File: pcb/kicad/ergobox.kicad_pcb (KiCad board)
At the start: 2 copper layers, 187.4 x 130.9 mm, 80 parts, among them SW1 SW_Push, SW10 Kailh, SW11 Kailh, SW12 Kailh, SW13 Kailh, SW14 Kailh, SW15 Kailh, SW16 Kailh, SW17 Kailh, SW18 Kailh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

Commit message: refactor: adjusts initial PCB layout to match viewlix specs
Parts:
- moved SW15 285.5 mm to (-102.5, 10.4), turned to -90 degrees
- moved C27 284.7 mm to (-111.3, 53.9), turned to -90 degrees
- moved D7 283.6 mm to (-110.1, 50.4), turned to -90 degrees
- moved R7 282.0 mm to (-109.4, 53.9), turned to -90 degrees
- moved C28 280.8 mm to (-108.8, 56.8), turned to -90 degrees
- moved U2 280.5 mm to (-107.0, 43.3), turned to -90 degrees
- moved SW20 278.4 mm to (-102.5, 28.6), turned to -90 degrees
- moved U1 278.0 mm to (-106.1, 50.5), turned to -90 degrees
- moved C4 277.8 mm to (-106.9, 59.0), turned to -90 degrees
- moved D3 276.6 mm to (-105.7, 55.6), turned to -90 degrees
- moved C2 275.9 mm to (-105.7, 61.9), turned to -90 degrees
- moved C1 275.0 mm to (-104.9, 59.0), turned to -90 degrees
- moved C18 273.1 mm to (-103.8, 61.9), turned to -90 degrees
- moved D5 269.2 mm to (-101.0, 61.8), turned to -90 degrees
- moved C26 267.9 mm to (-100.2, 65.3), turned to -90 degrees
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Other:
- board size 187.4 x 130.9 mm -> 234.6 x 145.7 mm

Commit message: feat: places kailh switches on PCB
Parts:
- moved SW20 346.7 mm to (240.6, 78.2), turned to 0 degrees
- moved SW15 308.9 mm to (204.2, 46.5), turned to 0 degrees
- moved SW16 308.4 mm to (239.5, 39.1), turned to 0 degrees
- moved SW19 280.1 mm to (205.4, 85.7), turned to 0 degrees
- moved SW14 254.8 mm to (169.0, 54.0), turned to 0 degrees
- moved SW17 248.9 mm to (140.8, 113.7), turned to 0 degrees
- moved SW9 241.8 mm to (125.5, 146.2), turned to 0 degrees
- moved SW18 227.0 mm to (170.2, 93.1), turned to 0 degrees
- moved SW13 197.1 mm to (139.7, 74.7), turned to 0 degrees
- moved C20 177.8 mm to (31.2, -39.5), turned to 0 degrees
- moved R6 173.9 mm to (28.4, -39.5), turned to 0 degrees
- moved C3 172.9 mm to (28.3, -37.5), turned to 0 degrees
- moved C8 172.0 mm to (28.3, -35.5), turned to 0 degrees
- moved C13 160.7 mm to (21.9, -29.3), turned to 0 degrees
- moved SW10 158.9 mm to (106.6, 80.0), turned to 0 degrees
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
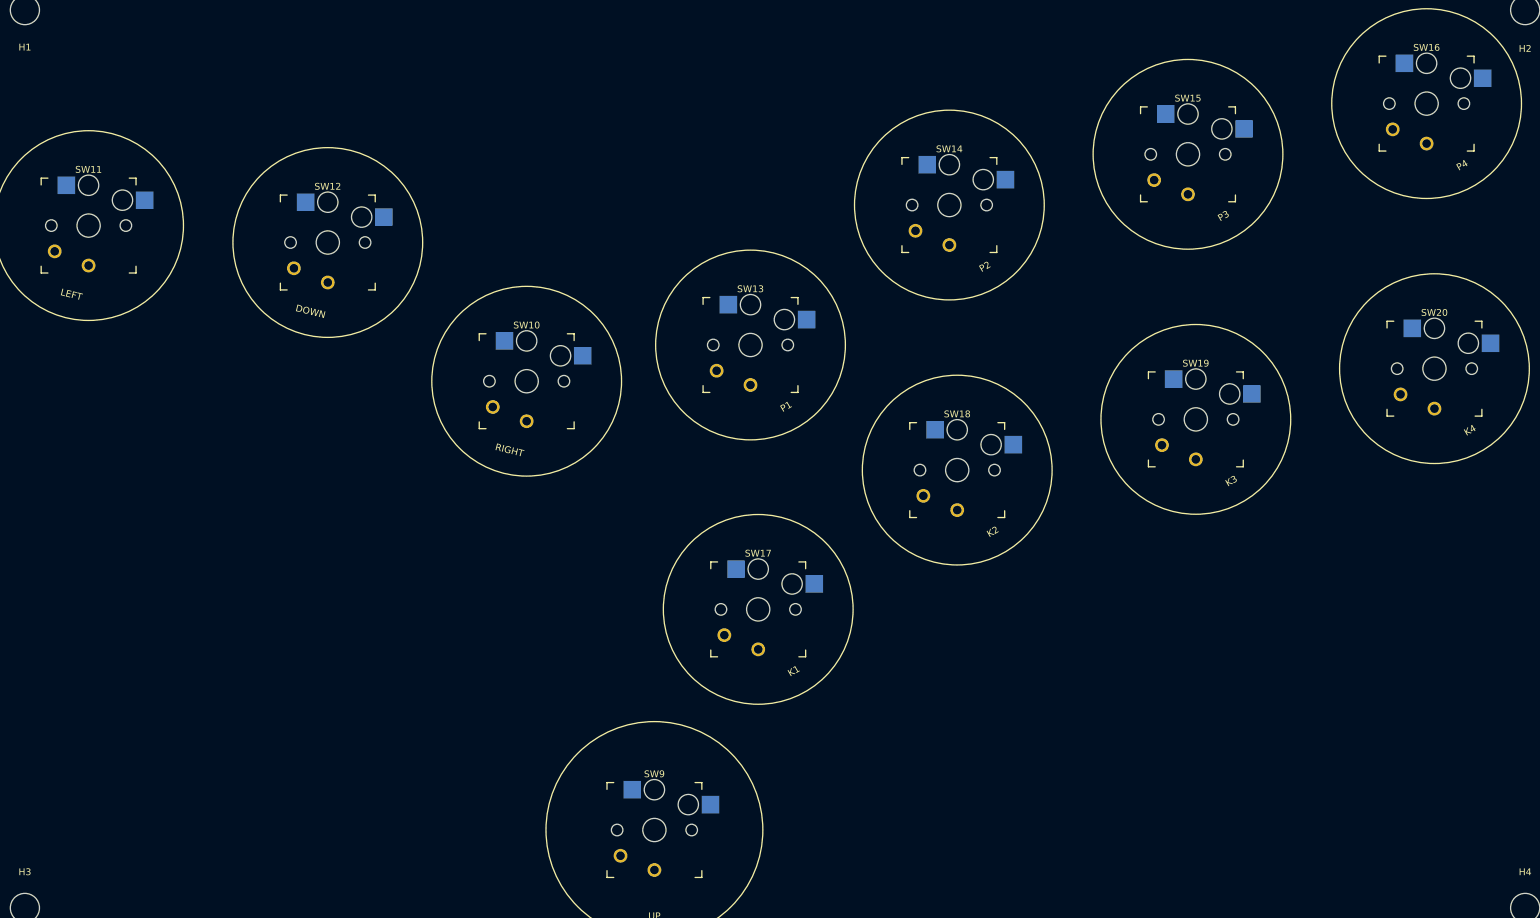
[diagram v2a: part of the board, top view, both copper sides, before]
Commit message: refactor: changes kailh footprints to hotswap non-optionals.
The kailh low footprints with optional hotswaps are not symmetric.
In the optional footprint, the hotswap switch pad goes through the RGB footpad,
so it cannot be used.
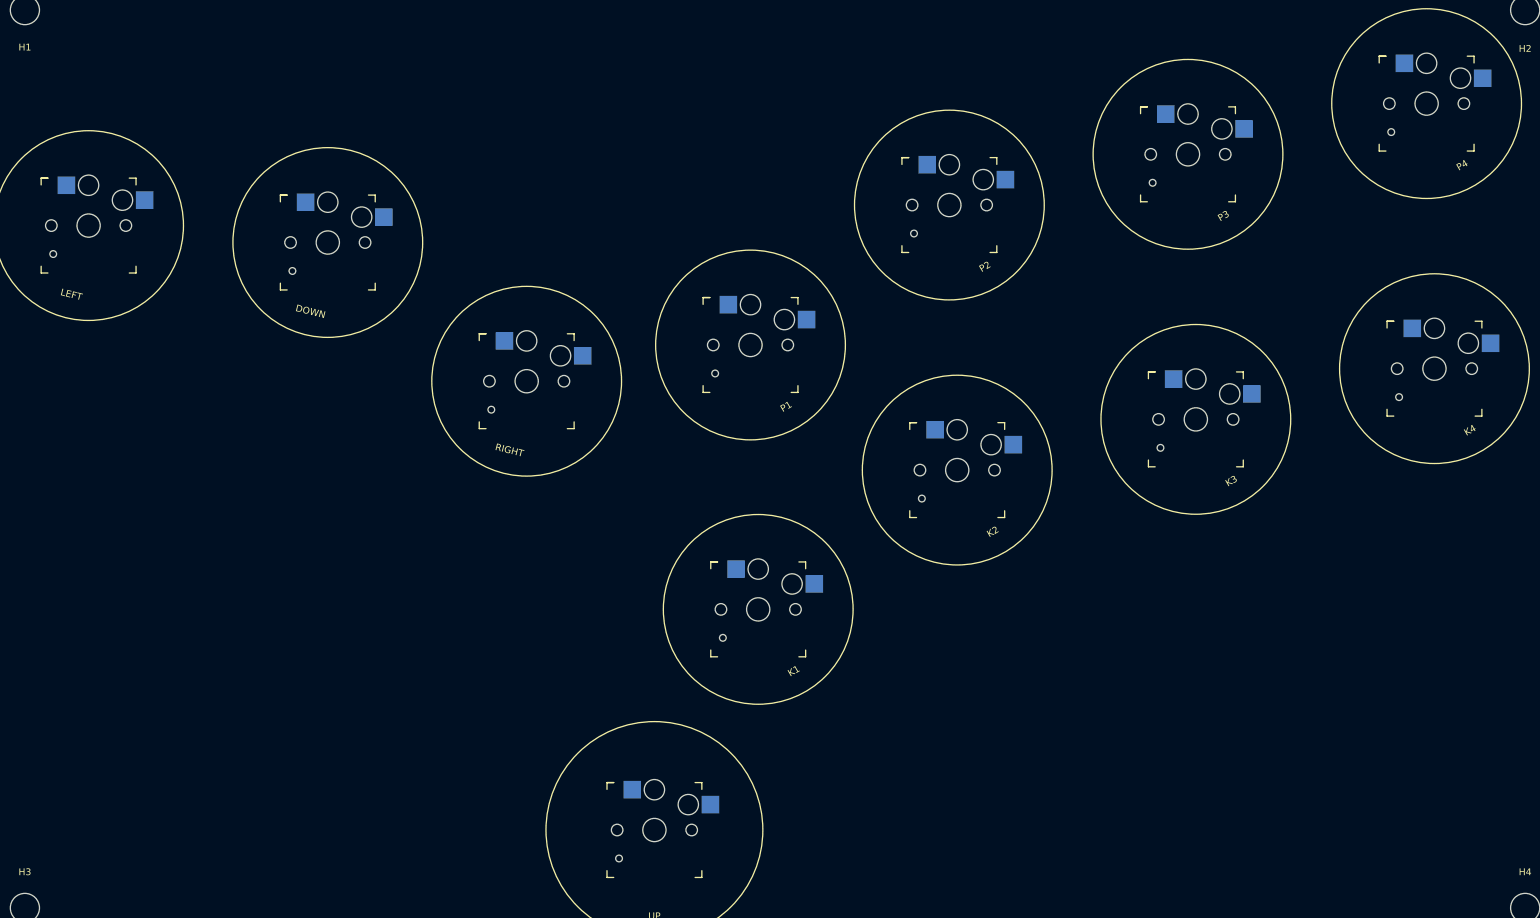
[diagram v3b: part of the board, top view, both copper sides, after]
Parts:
- SW10, SW11, SW12, SW13, SW14, SW15, SW16, SW17, SW18, SW19, SW20, SW9: footprint Keyswitches:Kailh_socket_PG1350_optional -> Keyswitches:Kailh_socket_PG1350
- turned SW10 to 180 degrees
- turned SW11 to 180 degrees
- turned SW12 to 180 degrees
- turned SW13 to 180 degrees
- turned SW14 to 180 degrees
- turned SW15 to 180 degrees
- turned SW16 to 180 degrees
- turned SW17 to 180 degrees
- turned SW18 to 180 degrees
- turned SW19 to 180 degrees
- turned SW20 to 180 degrees
- turned SW9 to 180 degrees

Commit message: feat: places per-key RGB LEDs on PCB
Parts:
- moved D7 279.8 mm to (239.5, 43.8), turned to 180 degrees
- moved D8 259.2 mm to (240.6, 82.9)
- moved D9 233.9 mm to (205.4, 90.3)
- moved D6 213.2 mm to (204.2, 51.2), turned to 180 degrees
- moved D10 209.1 mm to (170.2, 97.8)
- moved D12 206.2 mm to (125.5, 150.9)
- moved D5 201.7 mm to (169.0, 58.7), turned to 180 degrees
- moved D11 195.1 mm to (140.8, 118.4)
- moved D4 162.3 mm to (139.7, 79.4), turned to 180 degrees
- moved D3 154.6 mm to (106.6, 84.7), turned to 180 degrees
- moved D2 109.0 mm to (77.3, 64.2), turned to 180 degrees
- moved D1 83.7 mm to (42.0, 61.8), turned to 180 degrees

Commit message: feat: introduces GND plane on B.Cu
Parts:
- H5: footprint MountingHole:MountingHole_3.2mm_M3 -> MountingHole:MountingHole_4.3mm_M4
- moved H5 192.0 mm to (143.3, 25.5)
- moved H6 116.2 mm to (143.3, 157.8)
- moved USB1 75.1 mm to (61.6, 13.2), turned to 180 degrees
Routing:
- added copper zone on B.Cu, net GND
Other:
- board size 234.6 x 145.7 mm -> 234.6 x 150.2 mm
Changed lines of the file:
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@@
   )
   (footprint "MountingHole:MountingHole_4.3mm_M4" (layer "F.Cu")
-    (at 31.1 188)
+    (at 143.3 157.75)
     (descr "Mounting Hole 4.3mm, no annular, M4")
     (tags "mounting hole 4.3mm no annular m4")
@@
     (property "Sheetname" "")
     (attr exclude_from_pos_files)
-    (fp_text reference "H6" (at 0.2 5.6) (layer "F.SilkS")
+    (fp_text reference "H6" (at 0.2 -5.45) (layer "F.SilkS")
       (effects (font (size 1 1) (thickness 0.15)))
     )
@@
       (net 6 "+5V") (pinfunction "VDD") (pintype "power_in"))
   )
-  (footprint "MountingHole:MountingHole_3.2mm_M3" (layer "F.Cu")
-    (at 41 188)
-    (descr "Mounting Hole 3.2mm, no annular, M3")
-    (tags "mounting hole 3.2mm no annular m3")
+  (footprint "MountingHole:MountingHole_4.3mm_M4" (layer "F.Cu")
+    (at 143.3 25.5)
+    (descr "Mounting Hole 4.3mm, no annular, M4")
+    (tags "mounting hole 4.3mm no annular m4")
     (property "Sheetfile" "ergobox.kicad_sch")
     (property "Sheetname" "")
     (attr exclude_from_pos_files)
-    (fp_text reference "H5" (at 0 -4.2) (layer "F.SilkS")
-      (effects (font (size 1 1) (thickness 0.15)))
-    )
-    (fp_text value "MountingHole" (at 0 4.2) (layer "F.Fab")
-      (effects (font (size 1 1) (thickness 0.15)))
-    )
-    (fp_text user "${REFERENCE}" (at 0 0) (layer "F.Fab")
-      (effects (font (size 1 1) (thickness 0.15)))
-    )
-    (fp_circle (center 0 0) (end 3.2 0) (layer "Cmts.User") (width 0.15) (fill none))
-    (fp_circle (center 0 0) (end 3.45 0) (layer "F.CrtYd") (width 0.05) (fill none))
-    (pad "" np_thru_hole circle (at 0 0) (size 3.2 3.2) (drill 3.2) (layers *.Cu *.Mask))
+    (fp_text reference "H5" (at 0 5.8) (layer "F.SilkS")
+      (effects (font (size 1 1) (thickness 0.15)))
+    )
+    (fp_text value "MountingHole" (at 0 5.3) (layer "F.Fab")
+      (effects (font (size 1 1) (thickness 0.15)))
+    )
+    (fp_text user "${REFERENCE}" (at 0 0) (layer "F.Fab")
+      (effects (font (size 1 1) (thickness 0.15)))
+    )
+    (fp_circle (center 0 0) (end 4.3 0) (layer "Cmts.User") (width 0.15) (fill none))
+    (fp_circle (center 0 0) (end 4.55 0) (layer "F.CrtYd") (width 0.05) (fill none))
+    (pad "" np_thru_hole circle (at 0 0) (size 4.3 4.3) (drill 4.3) (layers *.Cu *.Mask))
   )
   (footprint "Capacitor_SMD:C_0402_1005Metric" (layer "F.Cu")
@@
   )
   (footprint "USB-C:HRO-TYPE-C-31-M-12" (layer "F.Cu")
-    (at 1.275 -31.555)
+    (at 61.6 13.215 180)
     (property "Sheetfile" "ergobox.kicad_sch")
     (property "Sheetname" "")
@@
     (fp_line (start -4.47 0) (end 4.47 0) (layer "Dwgs.User") (width 0.15))
     (fp_line (start 4.47 0) (end 4.47 -7.3) (layer "Dwgs.User") (width 0.15))
-    (pad "" np_thru_hole circle locked (at -2.89 -6.25) (size 0.65 0.65) (drill 0.65) (layers *.Cu *.Mask))
-    (pad "" np_thru_hole circle locked (at 2.89 -6.25) (size 0.65 0.65) (drill 0.65) (layers *.Cu *.Mask))
-    (pad "1" smd rect locked (at -3.225 -7.695) (size 0.6 1.45) (layers "F.Cu" "F.Paste" "F.Mask")
+    (pad "" np_thru_hole circle locked (at -2.89 -6.25 180) (size 0.65 0.65) (drill 0.65) (layers *.Cu *.Mask))
+    (pad "" np_thru_hole circle locked (at 2.89 -6.25 180) (size 0.65 0.65) (drill 0.65) (layers *.Cu *.Mask))
+    (pad "1" smd rect locked (at -3.225 -7.695 180) (size 0.6 1.45) (layers "F.Cu" "F.Paste" "F.Mask")
       (net 2 "GND") (pinfunction "GND") (pintype "input"))
-    (pad "2" smd rect locked (at -2.45 -7.695) (size 0.6 1.45) (layers "F.Cu" "F.Paste" "F.Mask")
+    (pad "2" smd rect locked (at -2.45 -7.695 180) (size 0.6 1.45) (layers "F.Cu" "F.Paste" "F.Mask")
       (net 6 "+5V") (pinfunction "VBUS") (pintype "input"))
-    (pad "3" smd rect locked (at -1.75 -7.695) (size 0.3 1.45) (layers "F.Cu" "F.Paste" "F.Mask")
+    (pad "3" smd rect locked (at -1.75 -7.695 180) (size 0.3 1.45) (layers "F.Cu" "F.Paste" "F.Mask")
       (net 68 "unconnected-(USB1-Pad3)") (pinfunction "SBU2") (pintype "input+no_connect"))
-    (pad "4" smd rect locked (at -1.25 -7.695) (size 0.3 1.45) (layers "F.Cu" "F.Paste" "F.Mask")
+    (pad "4" smd rect locked (at -1.25 -7.695 180) (size 0.3 1.45) (layers "F.Cu" "F.Paste" "F.Mask")
       (net 25 "Net-(R4-Pad1)") (pinfunction "CC1") (pintype "input"))
-    (pad "5" smd rect locked (at -0.75 -7.695) (size 0.3 1.45) (layers "F.Cu" "F.Paste" "F.Mask")
+    (pad "5" smd rect locked (at -0.75 -7.695 180) (size 0.3 1.45) (layers "F.Cu" "F.Paste" "F.Mask")
       (net 23 "USB_D-") (pinfunction "DN2") (pintype "input"))
-    (pad "6" smd rect locked (at -0.25 -7.695) (size 0.3 1.45) (layers "F.Cu" "F.Paste" "F.Mask")
+    (pad "6" smd rect locked (at -0.25 -7.695 180) (size 0.3 1.45) (layers "F.Cu" "F.Paste" "F.Mask")
       (net 21 "USB_D+") (pinfunction "DP1") (pintype "input"))
-    (pad "7" smd rect locked (at 0.25 -7.695) (size 0.3 1.45) (layers "F.Cu" "F.Paste" "F.Mask")
+    (pad "7" smd rect locked (at 0.25 -7.695 180) (size 0.3 1.45) (layers "F.Cu" "F.Paste" "F.Mask")
       (net 23 "USB_D-") (pinfunction "DN1") (pintype "input"))
-    (pad "8" smd rect locked (at 0.75 -7.695) (size 0.3 1.45) (layers "F.Cu" "F.Paste" "F.Mask")
+    (pad "8" smd rect locked (at 0.75 -7.695 180) (size 0.3 1.45) (layers "F.Cu" "F.Paste" "F.Mask")
       (net 21 "USB_D+") (pinfunction "DP2") (pintype "input"))
-    (pad "9" smd rect locked (at 1.25 -7.695) (size 0.3 1.45) (layers "F.Cu" "F.Paste" "F.Mask")
+    (pad "9" smd rect locked (at 1.25 -7.695 180) (size 0.3 1.45) (layers "F.Cu" "F.Paste" "F.Mask")
       (net 67 "unconnected-(USB1-Pad9)") (pinfunction "SBU1") (pintype "input+no_connect"))
-    (pad "10" smd rect locked (at 1.75 -7.695) (size 0.3 1.45) (layers "F.Cu" "F.Paste" "F.Mask")
+    (pad "10" smd rect locked (at 1.75 -7.695 180) (size 0.3 1.45) (layers "F.Cu" "F.Paste" "F.Mask")
       (net 24 "Net-(R3-Pad1)") (pinfunction "CC2") (pintype "input"))
-    (pad "11" smd rect locked (at 2.45 -7.695) (size 0.6 1.45) (layers "F.Cu" "F.Paste" "F.Mask")
+    (pad "11" smd rect locked (at 2.45 -7.695 180) (size 0.6 1.45) (layers "F.Cu" "F.Paste" "F.Mask")
       (net 6 "+5V") (pinfunction "VBUS") (pintype "input"))
-    (pad "12" smd rect locked (at 3.225 -7.695) (size 0.6 1.45) (layers "F.Cu" "F.Paste" "F.Mask")
+    (pad "12" smd rect locked (at 3.225 -7.695 180) (size 0.6 1.45) (layers "F.Cu" "F.Paste" "F.Mask")
       (net 2 "GND") (pinfunction "GND") (pintype "input"))
-    (pad "13" thru_hole oval locked (at 4.32 -2.6) (size 1 1.6) (drill oval 0.6 1.2) (layers *.Cu "B.Mask")
+    (pad "13" thru_hole oval locked (at 4.32 -2.6 180) (size 1 1.6) (drill oval 0.6 1.2) (layers *.Cu "B.Mask")
       (net 2 "GND") (pinfunction "SHIELD") (pintype "input"))
-    (pad "13" thru_hole oval locked (at 4.32 -6.78) (size 1 2.1) (drill oval 0.6 1.7) (layers *.Cu "B.Mask")
+    (pad "13" thru_hole oval locked (at 4.32 -6.78 180) (size 1 2.1) (drill oval 0.6 1.7) (layers *.Cu "B.Mask")
       (net 2 "GND") (pinfunction "SHIELD") (pintype "input"))
-    (pad "13" thru_hole oval locked (at -4.32 -6.78) (size 1 2.1) (drill oval 0.6 1.7) (layers *.Cu "B.Mask")
+    (pad "13" thru_hole oval locked (at -4.32 -6.78 180) (size 1 2.1) (drill oval 0.6 1.7) (layers *.Cu "B.Mask")
       (net 2 "GND") (pinfunction "SHIELD") (pintype "input"))
-    (pad "13" thru_hole oval locked (at -4.32 -2.6) (size 1 1.6) (drill oval 0.6 1.2) (layers *.Cu "B.Mask")
+    (pad "13" thru_hole oval locked (at -4.32 -2.6 180) (size 1 1.6) (drill oval 0.6 1.2) (layers *.Cu "B.Mask")
       (net 2 "GND") (pinfunction "SHIELD") (pintype "input"))
   )
@@
   (gr_line (start 139.7 74.65) (end 204.2 46.55) (layer "Cmts.User") (width 0.15))
   (gr_arc (start 32.6 164.3) (mid 27.95094 162.363973) (end 26.050188 157.70038) (layer "Edge.Cuts") (width 0.1))
-  (gr_line (start 254 18.65) (end 32.6 18.65) (layer "Edge.Cuts") (width 0.1))
+  (gr_line (start 55.1 18.65) (end 32.6 18.65) (layer "Edge.Cuts") (width 0.1))
+  (gr_arc (start 56.1 17.65) (mid 55.807107 18.357107) (end 55.1 18.65) (layer "Edge.Cuts") (width 0.1))
+  (gr_line (start 67.1 14.15) (end 67.1 17.65) (layer "Edge.Cuts") (width 0.1))
   (gr_arc (start 26 25.25) (mid 27.933095 20.583095) (end 32.6 18.65) (layer "Edge.Cuts") (width 0.1))
   (gr_arc (start 260.5 157.8) (mid 258.578618 162.363974) (end 254 164.250192) (layer "Edge.Cuts") (width 0.1))
   (gr_arc (start 254 18.65) (mid 258.666905 20.583095) (end 260.6 25.25) (layer "Edge.Cuts") (width 0.1))
   (gr_line (start 260.5 157.8) (end 260.6 25.25) (layer "Edge.Cuts") (width 0.1))
+  (gr_arc (start 68.1 18.65) (mid 67.392893 18.357107) (end 67.1 17.65) (layer "Edge.Cuts") (width 0.1))
+  (gr_line (start 56.1 17.65) (end 56.1 14.15) (layer "Edge.Cuts") (width 0.1))
   (gr_line (start 26 25.25) (end 26.050188 157.70038) (layer "Edge.Cuts") (width 0.1))
+  (gr_line (start 68.1 18.65) (end 254 18.65) (layer "Edge.Cuts") (width 0.1))
   (gr_line (start 32.6 164.3) (end 254 164.250192) (layer "Edge.Cuts") (width 0.1))
+  (gr_line (start 56.1 14.15) (end 67.1 14.15) (layer "Edge.Cuts") (width 0.1))
   (gr_text "UP" (at 125.5 158.95) (layer "F.SilkS")
     (effects (font (size 1 1) (thickness 0.15)))
@@
   (target plus (at 319.300001 116.2) (size 5) (width 0.1) (layer "Edge.Cuts"))
   (target plus (at 170.186685 93.134821) (size 5) (width 0.1) (layer "Edge.Cuts"))
+  (zone (net 2) (net_name "GND") (layer "B.Cu") (name "GND") (hatch edge 0.508)
+    (connect_pads (clearance 0.2))
+    (min_thickness 0.254) (filled_areas_thickness no)
+    (fill yes (thermal_gap 0.508) (thermal_bridge_width 0.508))
+    (polygon
+      (pts
+        (xy 264.403815 10.688347)
+        (xy 264.4 168)
+        (xy 22.5 168)
+        (xy 22.7 15.3)
+        (xy 22.603815 10.488347)
+      )
+    )
+  )
   (group "" (id 0035b4bf-bee4-4ef9-8b55-4f8fc902377c)
     (members

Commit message: feat: checkin milestone
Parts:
- C11: value 100n -> 1u
- moved SW8 124.6 mm to (74.8, 4.95), turned to 90 degrees
- moved SW5 114.7 mm to (83.3, -5.55), turned to 90 degrees
- moved SW6 110.8 mm to (91.7, 5.10), turned to 90 degrees
- moved U2 108.0 mm to (60.6, 33.2)
- moved SW4 106.7 mm to (83.2, 5.00), turned to 90 degrees
- moved SW7 106.5 mm to (74.8, -5.55), turned to 90 degrees
- moved C4 101.7 mm to (70.5, 24.3)
- moved SW3 97.4 mm to (91.8, -5.40), turned to 90 degrees
- moved SW1 97.1 mm to (68.8, -9.19), turned to 90 degrees
- moved SW2 87.3 mm to (68.8, 1.75), turned to 90 degrees
- moved C2 86.8 mm to (55.0, -2.42), turned to 90 degrees
- moved C11 85.0 mm to (64.2, 26.1), turned to 90 degrees
- moved R2 80.2 mm to (62.0, 26.1), turned to 90 degrees
- moved R3 75.8 mm to (58.9, 22.6), turned to 180 degrees
- moved U3 73.7 mm to (46.6, 24.3)
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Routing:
- net USB_D+: track 0.00 -> 7.92 mm
- net GND: track 0.00 -> 7.77 mm, vias 0 -> 1
- net USB_D-: track 0.00 -> 7.38 mm
- net +5V: track 0.00 -> 7.21 mm
- net +3V3: track 0.00 -> 3.74 mm
- net Net-(R1-Pad1): track 0.00 -> 3.46 mm
- net +1V1: track 0.00 -> 3.45 mm
- net Net-(R2-Pad1): track 0.00 -> 3.17 mm
- net Net-(R3-Pad1): track 0.00 -> 1.87 mm
- net Net-(R4-Pad1): track 0.00 -> 1.78 mm
- added copper zone on F.Cu, net GND

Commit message: feat: initial lay out for flash and power
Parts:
- moved C14 54.9 mm to (68.7, 22.0), turned to 180 degrees
- moved U1 49.1 mm to (68.2, 24.6), turned to -90 degrees
- moved C15 45.1 mm to (68.7, 27.2), turned to 180 degrees
- moved Y1 42.2 mm to (60.3, 41.5)
- moved C6 35.0 mm to (65.9, 34.6)
- moved C10 34.4 mm to (75.4, 30.8), turned to 90 degrees
- moved C1 34.0 mm to (58.7, 26.1), turned to 90 degrees
- moved C16 33.0 mm to (54.6, 21.5)
- moved C5 32.8 mm to (65.9, 30.4)
- moved C9 32.2 mm to (74.3, 30.8), turned to 90 degrees
- moved C7 26.8 mm to (55.2, 31.0), turned to 180 degrees
- moved R7 23.1 mm to (47.4, 21.5)
- moved C8 22.2 mm to (59.8, 26.1), turned to 90 degrees
- moved C4 6.79 mm to (65.9, 29.3)
- moved U3 4.00 mm to (50.5, 25.2)
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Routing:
- net +3V3: track 3.74 -> 68.8 mm, vias 0 -> 2
- net QSPI_SS: track 0.00 -> 24.9 mm
- net +1V1: track 3.45 -> 26.9 mm, vias 0 -> 4
- net QSPI_SD1: track 0.00 -> 21.9 mm
- net QSPI_SD2: track 0.00 -> 20.9 mm
- net GND: track 7.77 -> 20.4 mm, vias 1 -> 8
- net +5V: track 7.21 -> 16.9 mm
- net QSPI_SD3: track 0.00 -> 9.09 mm
- net QSPI_SCLK: track 0.00 -> 8.04 mm
- net QSPI_SD0: track 0.00 -> 7.34 mm
